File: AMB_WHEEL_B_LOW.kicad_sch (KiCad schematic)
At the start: 14 parts, among them U17 EPC2152, U18 EPC2152

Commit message: updated layouts, added motor
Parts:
- renumbered C119 to C143, C120 to C144, C121 to C145, C122 to C146, C123 to C147, C124 to C148, C125 to C149, C126 to C150, R83 to R139, R84 to R140, R85 to R141, R86 to R142, U17 to U15, U18 to U16

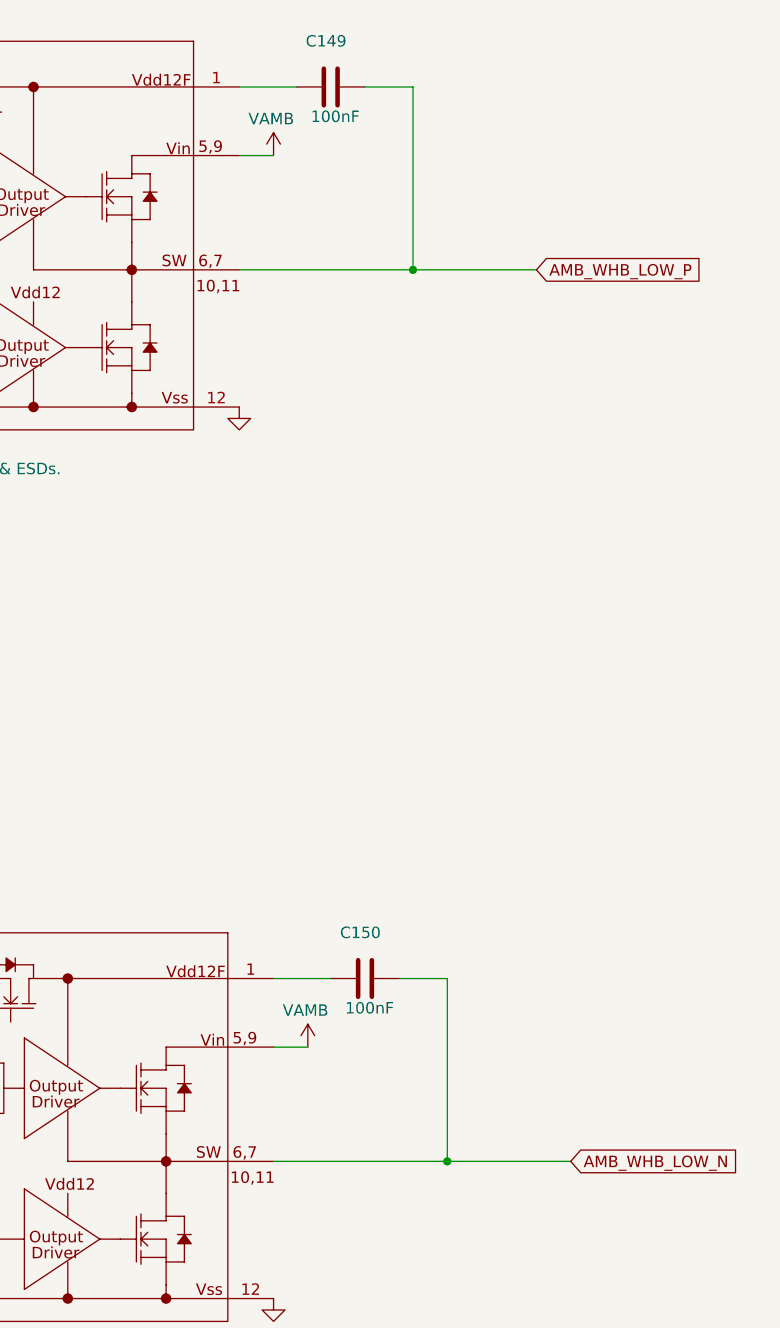
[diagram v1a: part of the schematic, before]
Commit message: Changes to layout pins
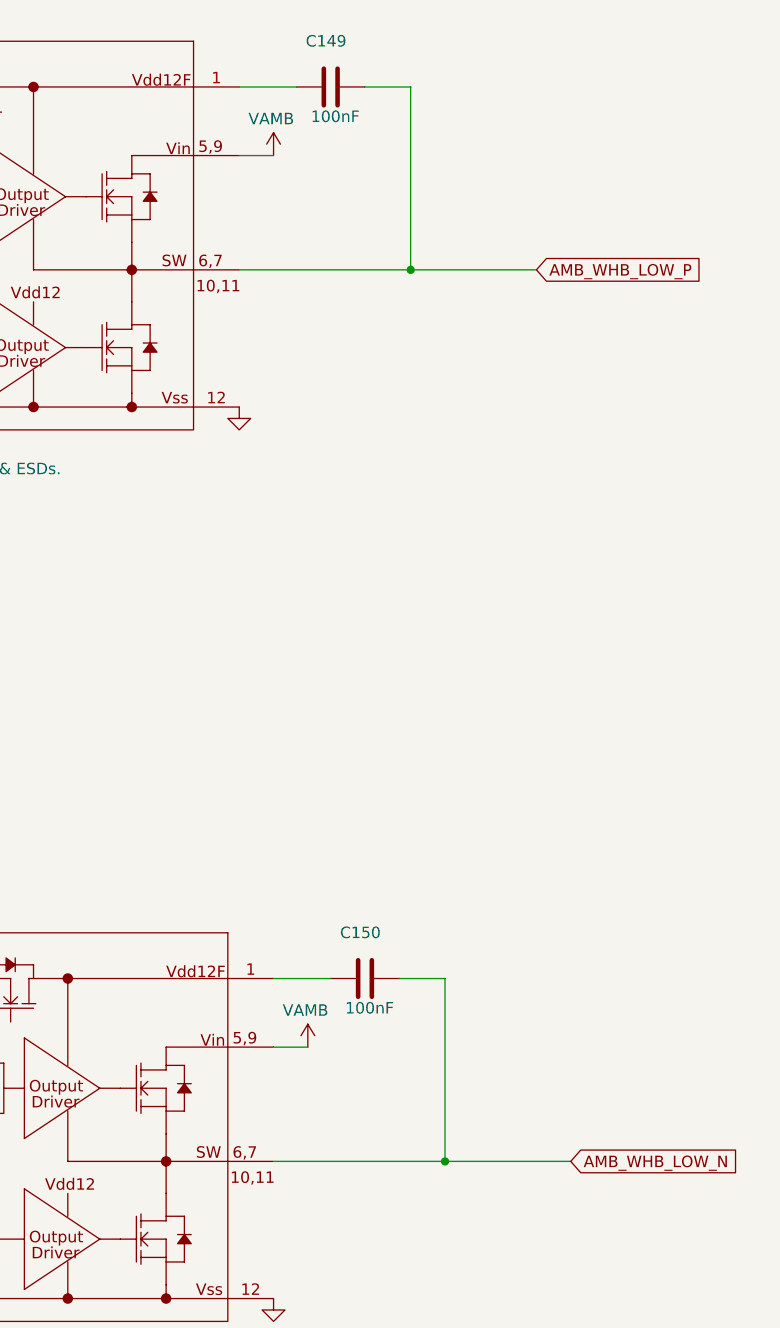
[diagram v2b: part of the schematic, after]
